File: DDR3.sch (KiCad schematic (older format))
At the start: 59 parts, among them U15 MT41K256M16HA-125_E, U16 MT41K256M16HA-125_E, U20 xc7z020clg484, U8 TPS51200DRCR

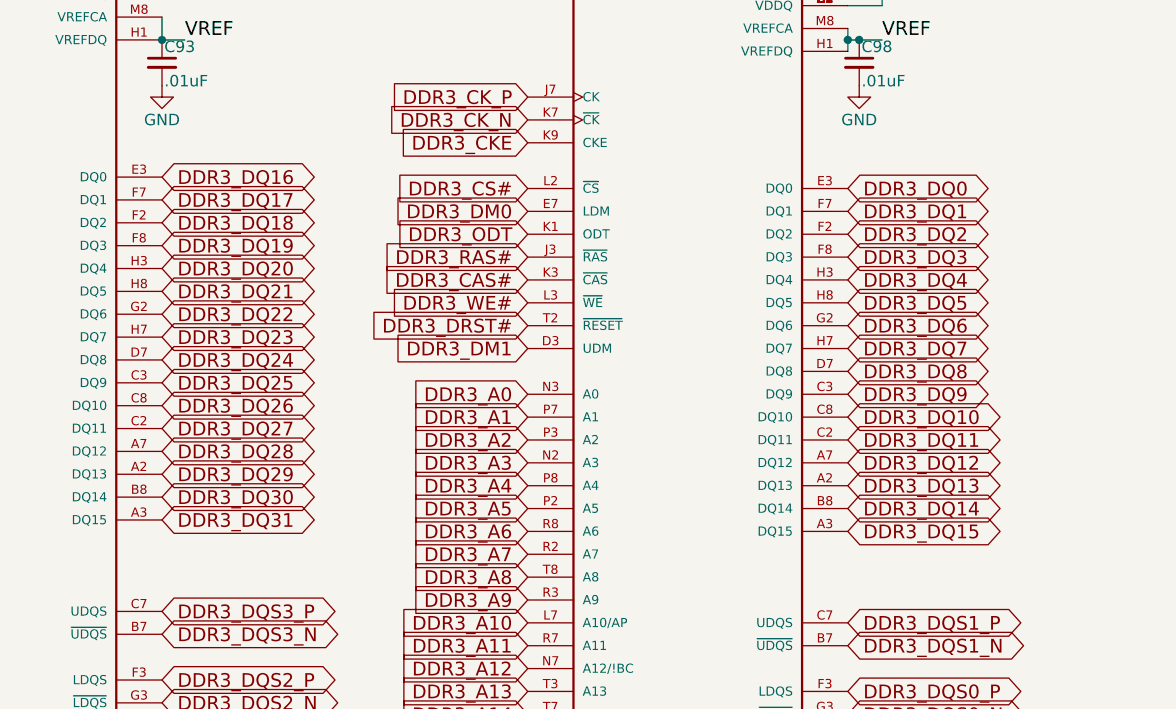
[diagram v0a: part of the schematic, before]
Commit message: finished DDR pinswaps, about to reposition chips closer to each other, and closer to the FPGA
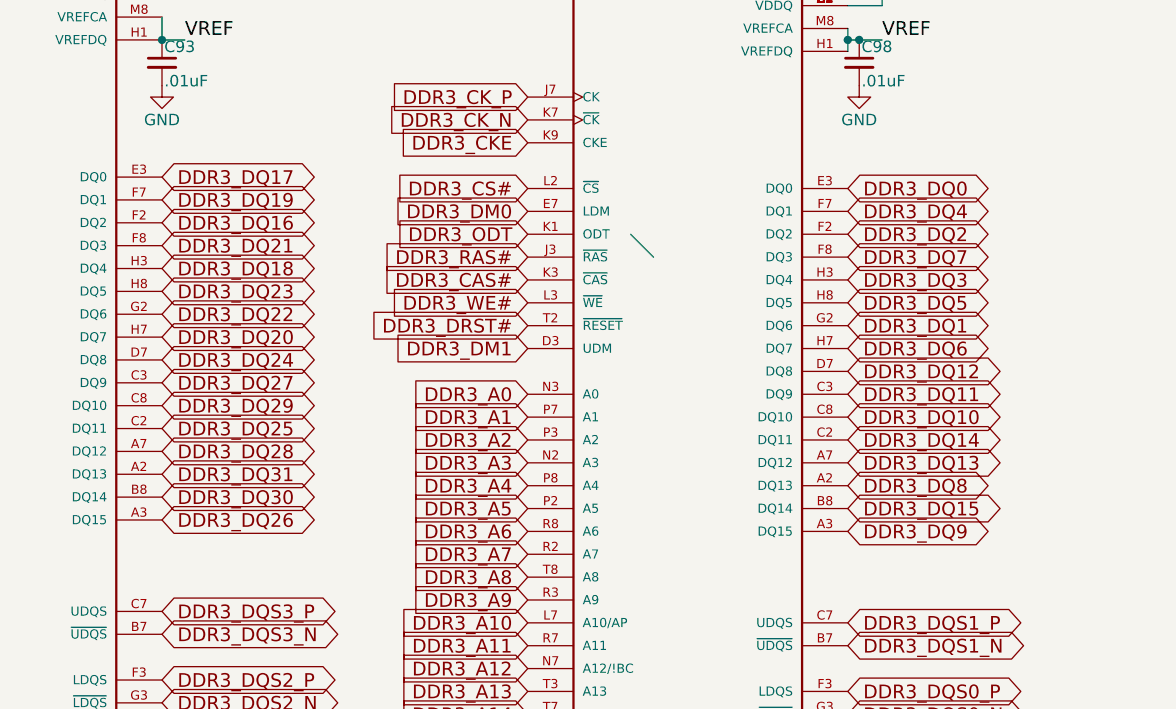
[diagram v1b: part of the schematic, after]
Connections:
- net DDR3_DQ1: now also U16.G2 (DQ6); no longer U16.F7 (DQ1)
- net DDR3_DQ11: now also U16.C3 (DQ9); no longer U16.C2 (DQ11)
- net DDR3_DQ12: now also U16.D7 (DQ8); no longer U16.A7 (DQ12)
- net DDR3_DQ13: now also U16.A7 (DQ12); no longer U16.A2 (DQ13)
- net DDR3_DQ14: now also U16.C2 (DQ11); no longer U16.B8 (DQ14)
- net DDR3_DQ15: now also U16.B8 (DQ14); no longer U16.A3 (DQ15)
- net DDR3_DQ16: now also U15.F2 (DQ2); no longer U15.E3 (DQ0)
- net DDR3_DQ17: now also U15.E3 (DQ0); no longer U15.F7 (DQ1)
- net DDR3_DQ18: now also U15.H3 (DQ4); no longer U15.F2 (DQ2)
- net DDR3_DQ19: now also U15.F7 (DQ1); no longer U15.F8 (DQ3)
- net DDR3_DQ20: now also U15.H7 (DQ7); no longer U15.H3 (DQ4)
- net DDR3_DQ21: now also U15.F8 (DQ3); no longer U15.H8 (DQ5)
- net DDR3_DQ23: now also U15.H8 (DQ5); no longer U15.H7 (DQ7)
- net DDR3_DQ25: now also U15.C2 (DQ11); no longer U15.C3 (DQ9)
- net DDR3_DQ26: now also U15.A3 (DQ15); no longer U15.C8 (DQ10)
- net DDR3_DQ27: now also U15.C3 (DQ9); no longer U15.C2 (DQ11)
- net DDR3_DQ29: now also U15.C8 (DQ10); no longer U15.A2 (DQ13)
- net DDR3_DQ3: now also U16.H3 (DQ4); no longer U16.F8 (DQ3)
- net DDR3_DQ31: now also U15.A2 (DQ13); no longer U15.A3 (DQ15)
- net DDR3_DQ4: now also U16.F7 (DQ1); no longer U16.H3 (DQ4)
- net DDR3_DQ6: now also U16.H7 (DQ7); no longer U16.G2 (DQ6)
- net DDR3_DQ7: now also U16.F8 (DQ3); no longer U16.H7 (DQ7)
- net DDR3_DQ8: now also U16.A2 (DQ13); no longer U16.D7 (DQ8)
- net DDR3_DQ9: now also U16.A3 (DQ15); no longer U16.C3 (DQ9)
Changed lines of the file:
@@
 Wire Wire Line
 	2800 7100 2500 7100
+Text GLabel 2500 2650 2    60   BiDi ~ 0
+DDR3_DQ16
 Text GLabel 2500 2450 2    60   BiDi ~ 0
-DDR3_DQ16
+DDR3_DQ17
+Text GLabel 2500 2850 2    60   BiDi ~ 0
+DDR3_DQ18
 Text GLabel 2500 2550 2    60   BiDi ~ 0
-DDR3_DQ17
-Text GLabel 2500 2650 2    60   BiDi ~ 0
-DDR3_DQ18
+DDR3_DQ19
+Text GLabel 2500 3150 2    60   BiDi ~ 0
+DDR3_DQ20
 Text GLabel 2500 2750 2    60   BiDi ~ 0
-DDR3_DQ19
-Text GLabel 2500 2850 2    60   BiDi ~ 0
-DDR3_DQ20
-Text GLabel 2500 2950 2    60   BiDi ~ 0
 DDR3_DQ21
 Text GLabel 2500 3050 2    60   BiDi ~ 0
 DDR3_DQ22
-Text GLabel 2500 3150 2    60   BiDi ~ 0
+Text GLabel 2500 2950 2    60   BiDi ~ 0
 DDR3_DQ23
 Text GLabel 2500 3250 2    60   BiDi ~ 0
 DDR3_DQ24
+Text GLabel 2500 3550 2    60   BiDi ~ 0
+DDR3_DQ25
+Text GLabel 2500 3950 2    60   BiDi ~ 0
+DDR3_DQ26
 Text GLabel 2500 3350 2    60   BiDi ~ 0
-DDR3_DQ25
-Text GLabel 2500 3450 2    60   BiDi ~ 0
-DDR3_DQ26
-Text GLabel 2500 3550 2    60   BiDi ~ 0
 DDR3_DQ27
 Text GLabel 2500 3650 2    60   BiDi ~ 0
 DDR3_DQ28
-Text GLabel 2500 3750 2    60   BiDi ~ 0
+Text GLabel 2500 3450 2    60   BiDi ~ 0
 DDR3_DQ29
 Text GLabel 2500 3850 2    60   BiDi ~ 0
 DDR3_DQ30
-Text GLabel 2500 3950 2    60   BiDi ~ 0
+Text GLabel 2500 3750 2    60   BiDi ~ 0
 DDR3_DQ31
 Text GLabel 2500 4650 2    60   BiDi ~ 0
@@
 Text GLabel 5500 4700 2    60   BiDi ~ 0
 DDR3_DQS0_P
-Text GLabel 5500 4000 2    60   BiDi ~ 0
+Text GLabel 5500 3900 2    60   BiDi ~ 0
 DDR3_DQ15
-Text GLabel 5500 3900 2    60   BiDi ~ 0
+Text GLabel 5500 3600 2    60   BiDi ~ 0
 DDR3_DQ14
-Text GLabel 5500 3800 2    60   BiDi ~ 0
+Text GLabel 5500 3700 2    60   BiDi ~ 0
 DDR3_DQ13
-Text GLabel 5500 3700 2    60   BiDi ~ 0
+Text GLabel 5500 3300 2    60   BiDi ~ 0
 DDR3_DQ12
-Text GLabel 5500 3600 2    60   BiDi ~ 0
+Text GLabel 5500 3400 2    60   BiDi ~ 0
 DDR3_DQ11
 Text GLabel 5500 3500 2    60   BiDi ~ 0
 DDR3_DQ10
-Text GLabel 5500 3400 2    60   BiDi ~ 0
+Text GLabel 5500 4000 2    60   BiDi ~ 0
 DDR3_DQ9
-Text GLabel 5500 3300 2    60   BiDi ~ 0
+Text GLabel 5500 3800 2    60   BiDi ~ 0
 DDR3_DQ8
+Text GLabel 5500 2800 2    60   BiDi ~ 0
+DDR3_DQ7
 Text GLabel 5500 3200 2    60   BiDi ~ 0
-DDR3_DQ7
-Text GLabel 5500 3100 2    60   BiDi ~ 0
 DDR3_DQ6
 Text GLabel 5500 3000 2    60   BiDi ~ 0
 DDR3_DQ5
+Text GLabel 5500 2600 2    60   BiDi ~ 0
+DDR3_DQ4
 Text GLabel 5500 2900 2    60   BiDi ~ 0
-DDR3_DQ4
-Text GLabel 5500 2800 2    60   BiDi ~ 0
 DDR3_DQ3
 Text GLabel 5500 2700 2    60   BiDi ~ 0
 DDR3_DQ2
-Text GLabel 5500 2600 2    60   BiDi ~ 0
+Text GLabel 5500 3100 2    60   BiDi ~ 0
 DDR3_DQ1
 Text GLabel 5500 2500 2    60   BiDi ~ 0
@@
 Wire Wire Line
 	3750 7300 4700 7300
+Entry Wire Line
+	4550 2700 4650 2800
 $EndSCHEMATC

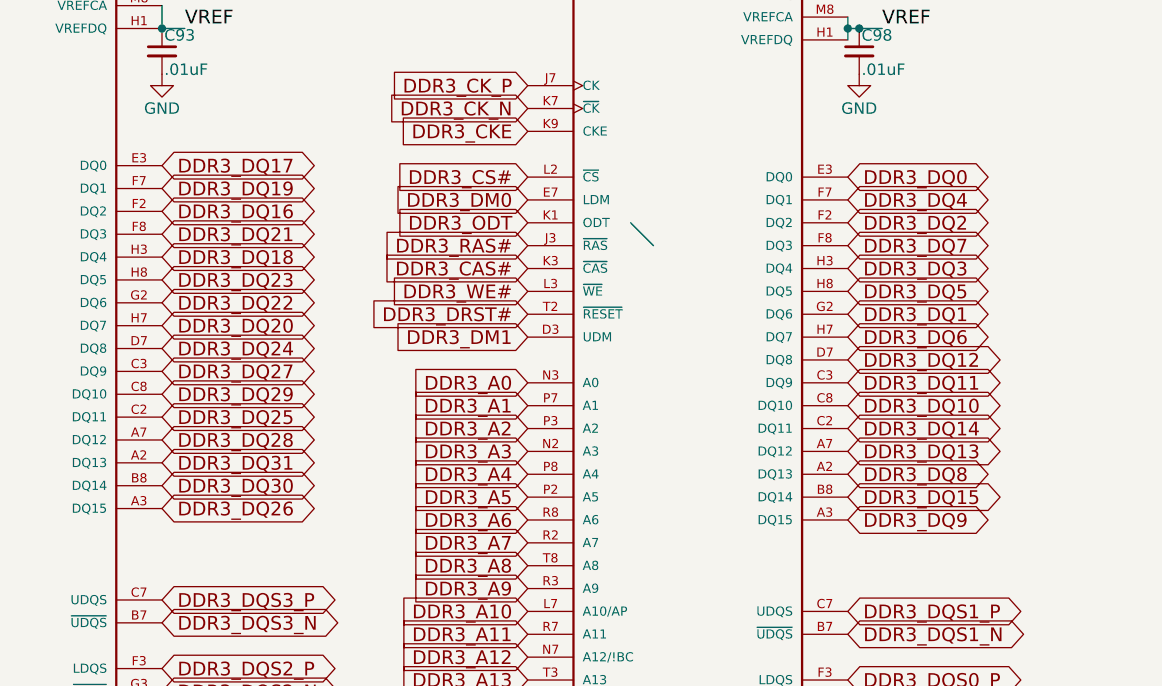
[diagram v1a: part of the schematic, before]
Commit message: low 2 ddr3 bytes delay matched WRT package flight time
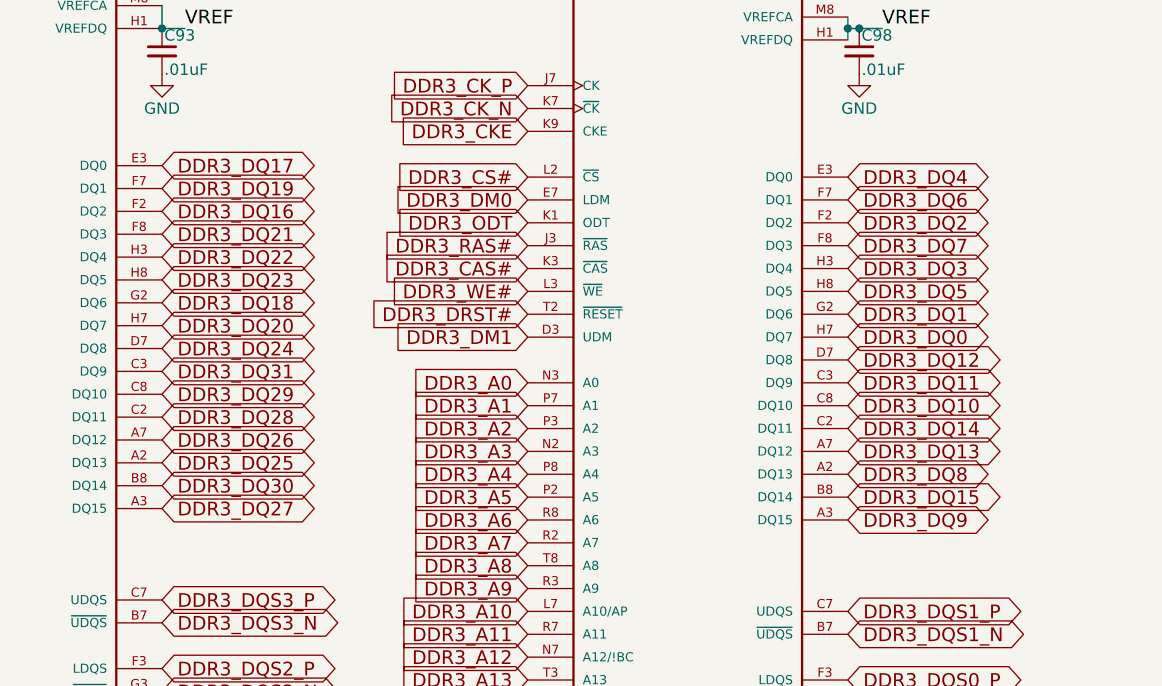
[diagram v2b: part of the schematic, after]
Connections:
- net DDR3_DQ0: now also U16.H7 (DQ7); no longer U16.E3 (DQ0)
- net DDR3_DQ18: now also U15.G2 (DQ6); no longer U15.H3 (DQ4)
- net DDR3_DQ22: now also U15.H3 (DQ4); no longer U15.G2 (DQ6)
- net DDR3_DQ25: now also U15.A2 (DQ13); no longer U15.C2 (DQ11)
- net DDR3_DQ26: now also U15.A7 (DQ12); no longer U15.A3 (DQ15)
- net DDR3_DQ27: now also U15.A3 (DQ15); no longer U15.C3 (DQ9)
- net DDR3_DQ28: now also U15.C2 (DQ11); no longer U15.A7 (DQ12)
- net DDR3_DQ31: now also U15.C3 (DQ9); no longer U15.A2 (DQ13)
- net DDR3_DQ4: now also U16.E3 (DQ0); no longer U16.F7 (DQ1)
- net DDR3_DQ6: now also U16.F7 (DQ1); no longer U16.H7 (DQ7)
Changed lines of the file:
@@
 Text GLabel 2500 2450 2    60   BiDi ~ 0
 DDR3_DQ17
-Text GLabel 2500 2850 2    60   BiDi ~ 0
+Text GLabel 2500 3050 2    60   BiDi ~ 0
 DDR3_DQ18
 Text GLabel 2500 2550 2    60   BiDi ~ 0
@@
 Text GLabel 2500 2750 2    60   BiDi ~ 0
 DDR3_DQ21
-Text GLabel 2500 3050 2    60   BiDi ~ 0
+Text GLabel 2500 2850 2    60   BiDi ~ 0
 DDR3_DQ22
 Text GLabel 2500 2950 2    60   BiDi ~ 0
@@
 Text GLabel 2500 3250 2    60   BiDi ~ 0
 DDR3_DQ24
+Text GLabel 2500 3750 2    60   BiDi ~ 0
+DDR3_DQ25
+Text GLabel 2500 3650 2    60   BiDi ~ 0
+DDR3_DQ26
+Text GLabel 2500 3950 2    60   BiDi ~ 0
+DDR3_DQ27
 Text GLabel 2500 3550 2    60   BiDi ~ 0
-DDR3_DQ25
-Text GLabel 2500 3950 2    60   BiDi ~ 0
-DDR3_DQ26
-Text GLabel 2500 3350 2    60   BiDi ~ 0
-DDR3_DQ27
-Text GLabel 2500 3650 2    60   BiDi ~ 0
 DDR3_DQ28
 Text GLabel 2500 3450 2    60   BiDi ~ 0
@@
 Text GLabel 2500 3850 2    60   BiDi ~ 0
 DDR3_DQ30
-Text GLabel 2500 3750 2    60   BiDi ~ 0
+Text GLabel 2500 3350 2    60   BiDi ~ 0
 DDR3_DQ31
 Text GLabel 2500 4650 2    60   BiDi ~ 0
@@
 Text GLabel 5500 2800 2    60   BiDi ~ 0
 DDR3_DQ7
-Text GLabel 5500 3200 2    60   BiDi ~ 0
+Text GLabel 5500 2600 2    60   BiDi ~ 0
 DDR3_DQ6
 Text GLabel 5500 3000 2    60   BiDi ~ 0
 DDR3_DQ5
-Text GLabel 5500 2600 2    60   BiDi ~ 0
+Text GLabel 5500 2500 2    60   BiDi ~ 0
 DDR3_DQ4
 Text GLabel 5500 2900 2    60   BiDi ~ 0
@@
 Text GLabel 5500 3100 2    60   BiDi ~ 0
 DDR3_DQ1
-Text GLabel 5500 2500 2    60   BiDi ~ 0
+Text GLabel 5500 3200 2    60   BiDi ~ 0
 DDR3_DQ0
 $Comp
@@
 Wire Wire Line
 	3750 7300 4700 7300
-Entry Wire Line
-	4550 2700 4650 2800
 $EndSCHEMATC

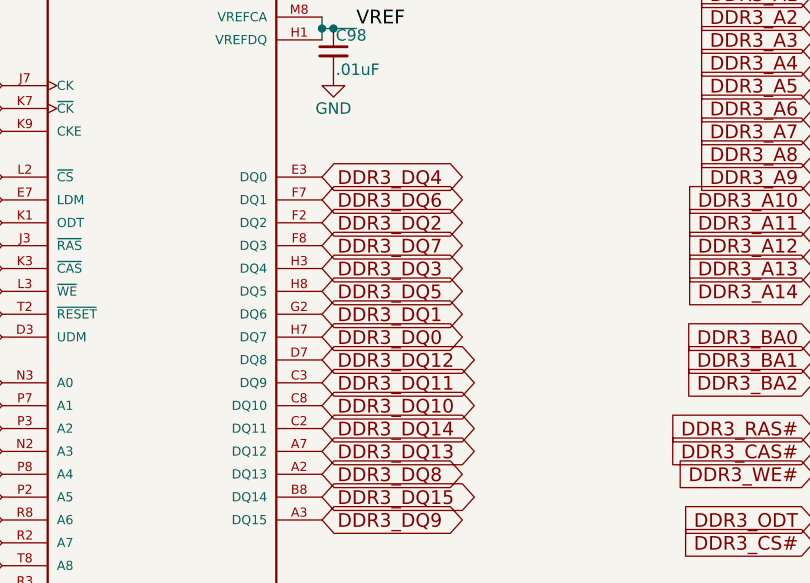
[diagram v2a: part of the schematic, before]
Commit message: widened serpentine routing consistant with guidelines (3x trace-to-plane) need to do data byte 2 and all address lines
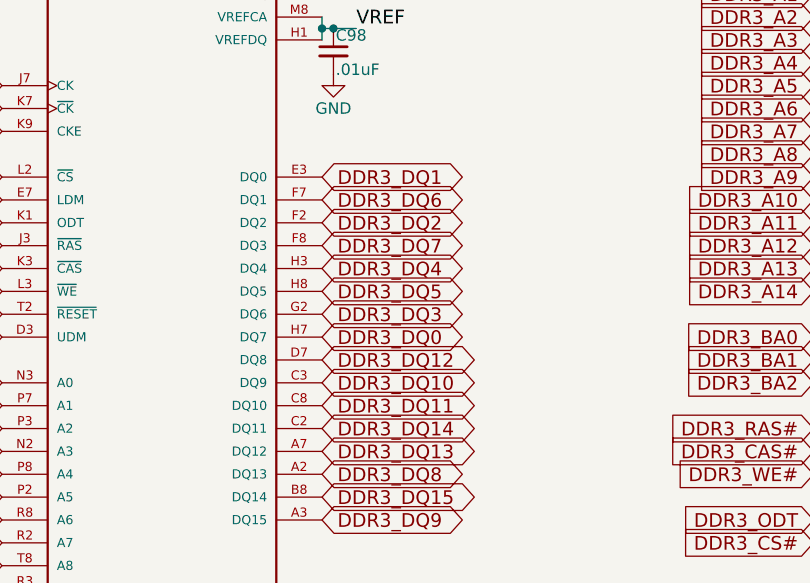
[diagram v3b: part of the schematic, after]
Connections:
- net DDR3_DQ1: now also U16.E3 (DQ0); no longer U16.G2 (DQ6)
- net DDR3_DQ10: now also U16.C3 (DQ9); no longer U16.C8 (DQ10)
- net DDR3_DQ11: now also U16.C8 (DQ10); no longer U16.C3 (DQ9)
- net DDR3_DQ3: now also U16.G2 (DQ6); no longer U16.H3 (DQ4)
- net DDR3_DQ4: now also U16.H3 (DQ4); no longer U16.E3 (DQ0)
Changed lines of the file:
@@
 Text GLabel 5500 3300 2    60   BiDi ~ 0
 DDR3_DQ12
+Text GLabel 5500 3500 2    60   BiDi ~ 0
+DDR3_DQ11
 Text GLabel 5500 3400 2    60   BiDi ~ 0
-DDR3_DQ11
-Text GLabel 5500 3500 2    60   BiDi ~ 0
 DDR3_DQ10
 Text GLabel 5500 4000 2    60   BiDi ~ 0
@@
 Text GLabel 5500 3000 2    60   BiDi ~ 0
 DDR3_DQ5
-Text GLabel 5500 2500 2    60   BiDi ~ 0
+Text GLabel 5500 2900 2    60   BiDi ~ 0
 DDR3_DQ4
-Text GLabel 5500 2900 2    60   BiDi ~ 0
-DDR3_DQ3
 Text GLabel 5500 2700 2    60   BiDi ~ 0
 DDR3_DQ2
-Text GLabel 5500 3100 2    60   BiDi ~ 0
-DDR3_DQ1
 Text GLabel 5500 3200 2    60   BiDi ~ 0
 DDR3_DQ0
@@
 Wire Wire Line
 	3750 7300 4700 7300
+Text GLabel 5500 2500 2    60   BiDi ~ 0
+DDR3_DQ1
+Text GLabel 5500 3100 2    60   BiDi ~ 0
+DDR3_DQ3
 $EndSCHEMATC

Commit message: finished ddr length matching git add -A!
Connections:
- net ZQL: now reaches R49.1, U16.L8 (ZQ)
- net ZQH: now reaches R46.1, U15.L8 (ZQ)
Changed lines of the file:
@@
 Text GLabel 5500 3100 2    60   BiDi ~ 0
 DDR3_DQ3
+Text Label 900  5350 0    59   ~ 0
+ZQH
+Text Label 3950 5400 0    59   ~ 0
+ZQL
 $EndSCHEMATC

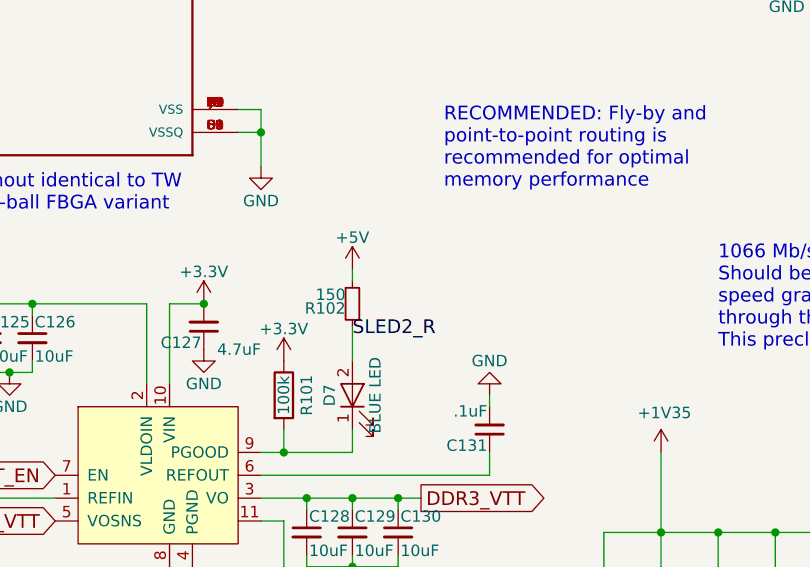
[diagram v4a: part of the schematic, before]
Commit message: about to remove ZIF screen connector in favor of UNO + RPI
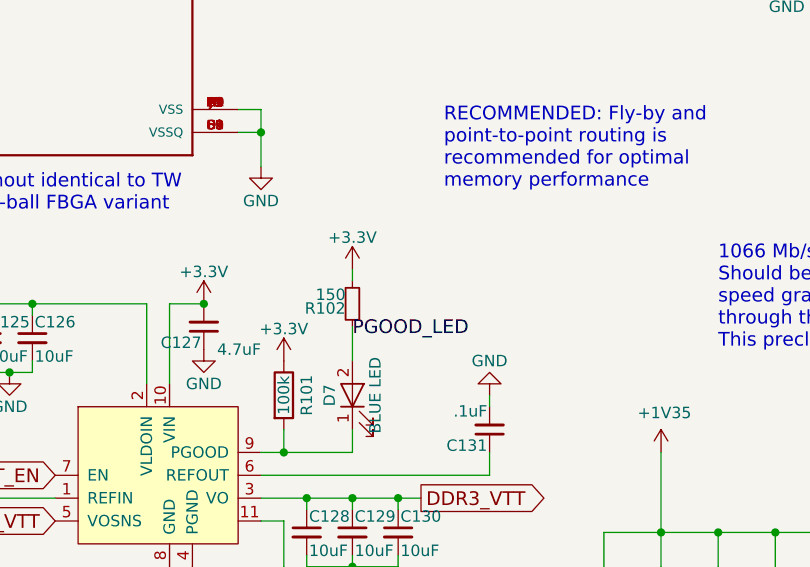
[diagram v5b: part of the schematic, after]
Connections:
- net +5V is gone; now on net +3V3: R102.2
- net SLED2_R renamed PGOOD_LED
